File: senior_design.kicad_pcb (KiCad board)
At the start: 2 copper layers, 128.6 x 80.8 mm, 41 parts, among them J1 Conn_ARM_JTAG_SWD_20, J4 USB_B_Micro, U11 NCP1117-3.3_SOT223, U2 OPA196xDGK, U3 SM351LT, U4 OPA196xDGK, U6 STM32F469VETx

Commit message: layout work
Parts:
- removed C13, C14, C15, C16: .1uF, Capacitor_SMD:C_0805_2012Metric
- removed U3: SM351LT, Package_TO_SOT_SMD:SOT-23
- added J2: Conn_01x03_Pin, Connector_PinHeader_2.54mm:PinHeader_1x03_P2.54mm_Vertical, F.Cu at (189.5, 129.0)
- moved C4 46.0 mm to (205.6, 87.5)
- moved C3 42.9 mm to (197.0, 96.0), turned to -90 degrees
- moved C8 42.2 mm to (205.4, 83.5)
- moved C7 34.0 mm to (199.0, 73.0), turned to 90 degrees
- moved C2 29.7 mm to (182.5, 90.0), turned to 180 degrees
- moved C1 27.0 mm to (182.0, 83.5)
- moved C5 23.6 mm to (183.0, 87.5), turned to 180 degrees
- moved C11 22.4 mm to (187.5, 73.0), turned to 90 degrees
- moved R3 20.5 mm to (196.0, 118.0)
- moved R8 20.3 mm to (192.5, 107.0), turned to -90 degrees
- moved R4 18.3 mm to (188.5, 125.5), turned to -90 degrees
- moved C9 17.6 mm to (182.5, 77.5), turned to 180 degrees
- moved C12 16.8 mm to (182.5, 80.5), turned to 180 degrees
- moved R7 13.3 mm to (189.0, 110.5)
- moved C17 10.7 mm to (177.5, 70.5), turned to 180 degrees
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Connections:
- C5 pad 1: +3.3V -> Net-(U6-VDDA)
- U6 pad 28: unconnected-(U6-PA7-Pad28) -> ADC_IN1
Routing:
- net /MCU/SWCLK: track 0.00 -> 55.1 mm, vias 0 -> 1
- net GND: track 0.00 -> 50.6 mm, vias 0 -> 28
- net /MCU/SWDIO: track 0.00 -> 48.6 mm
- net +3.3V: track 0.00 -> 35.8 mm
- net ADC_IN1: track 0.00 -> 23.7 mm
- net +5V: track 0.00 -> 16.5 mm
- net Net-(U4-+): track 0.00 -> 15.8 mm
- net Net-(U2--): track 0.00 -> 10.1 mm
- net Net-(R11-Pad1): track 0.00 -> 8.77 mm
- net Net-(U2-+): track 0.00 -> 8.68 mm
- net Net-(U4--): track 0.00 -> 8.33 mm
- net Net-(U6-VDDA): track 0.00 -> 7.88 mm
- net Net-(J2-Pin_2): track 0.00 -> 4.61 mm
- net /MCU/SWD_RESET: track 0.00 -> 3.07 mm
- net Net-(D1-A): track 0.00 -> 2.85 mm
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- added copper zone on F.Cu, net +3.3V
- added copper zone on B.Cu, net GND

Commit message: schematic finish
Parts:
- added U3: RA8875, ra8875:RA8875, F.Cu at (229.9, 115.7)
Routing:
- net +5V: track 16.5 -> 88.0 mm, vias 0 -> 2
- net /MCU/SWCLK: vias 1 -> 2

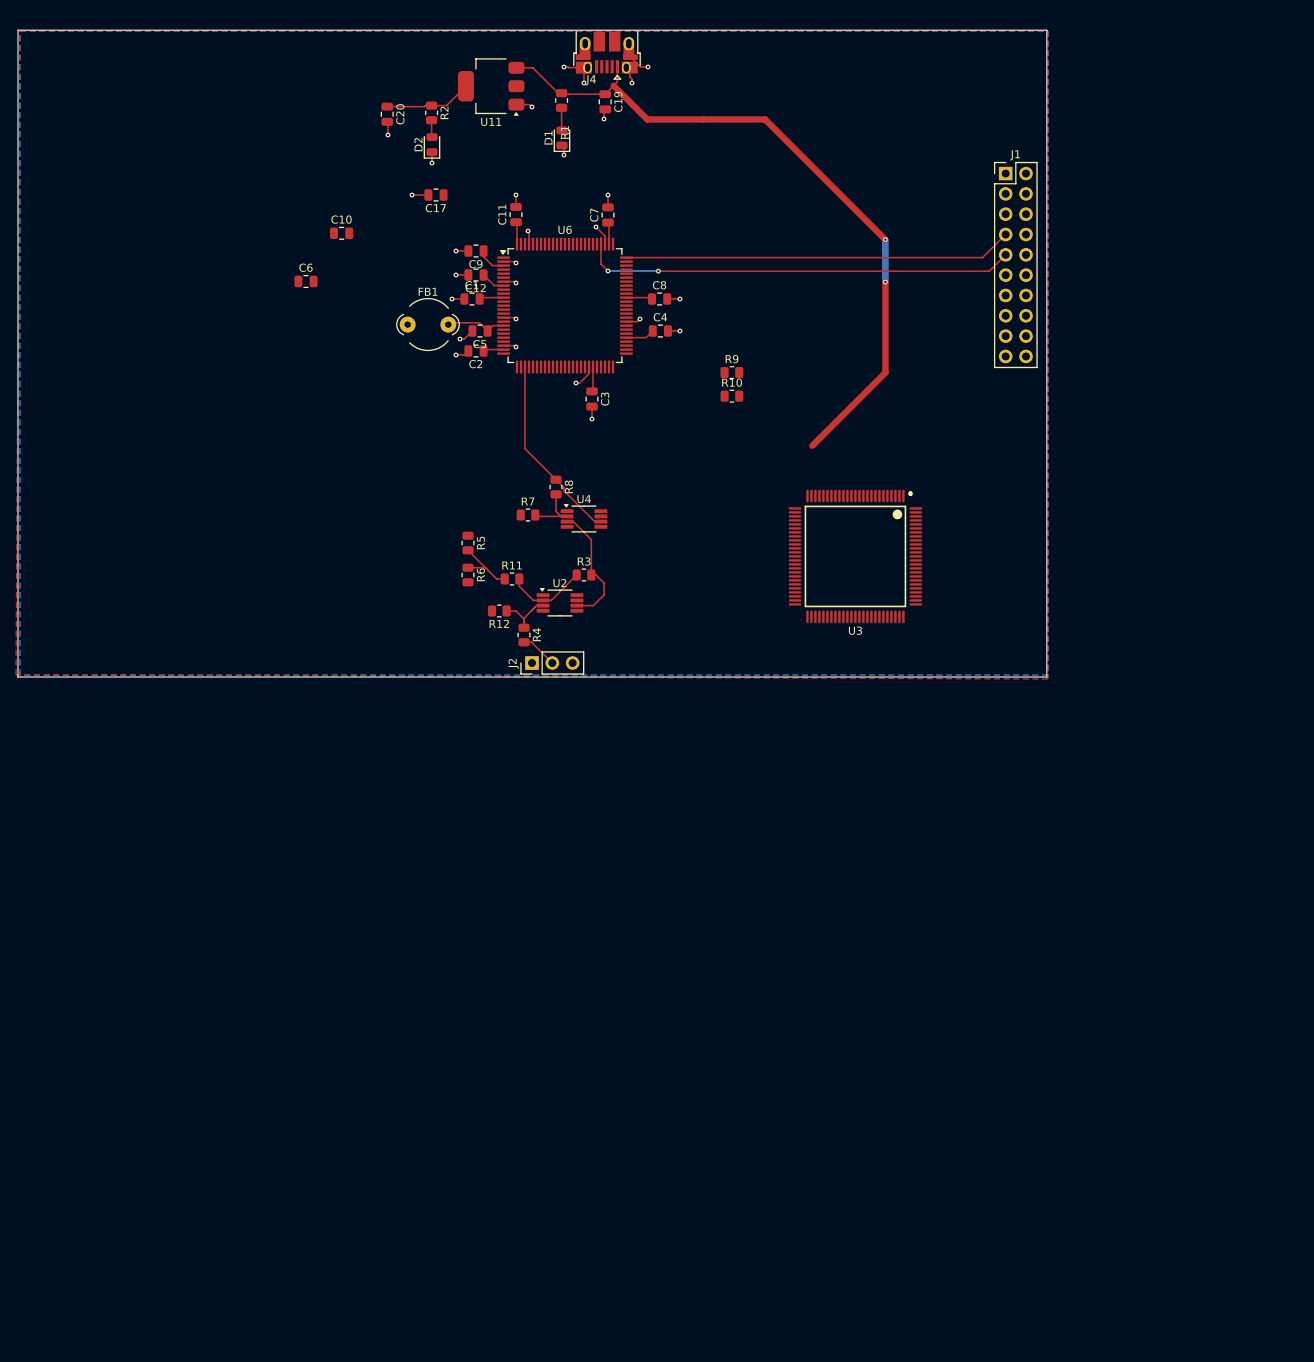
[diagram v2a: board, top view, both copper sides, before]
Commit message: initial display pcb
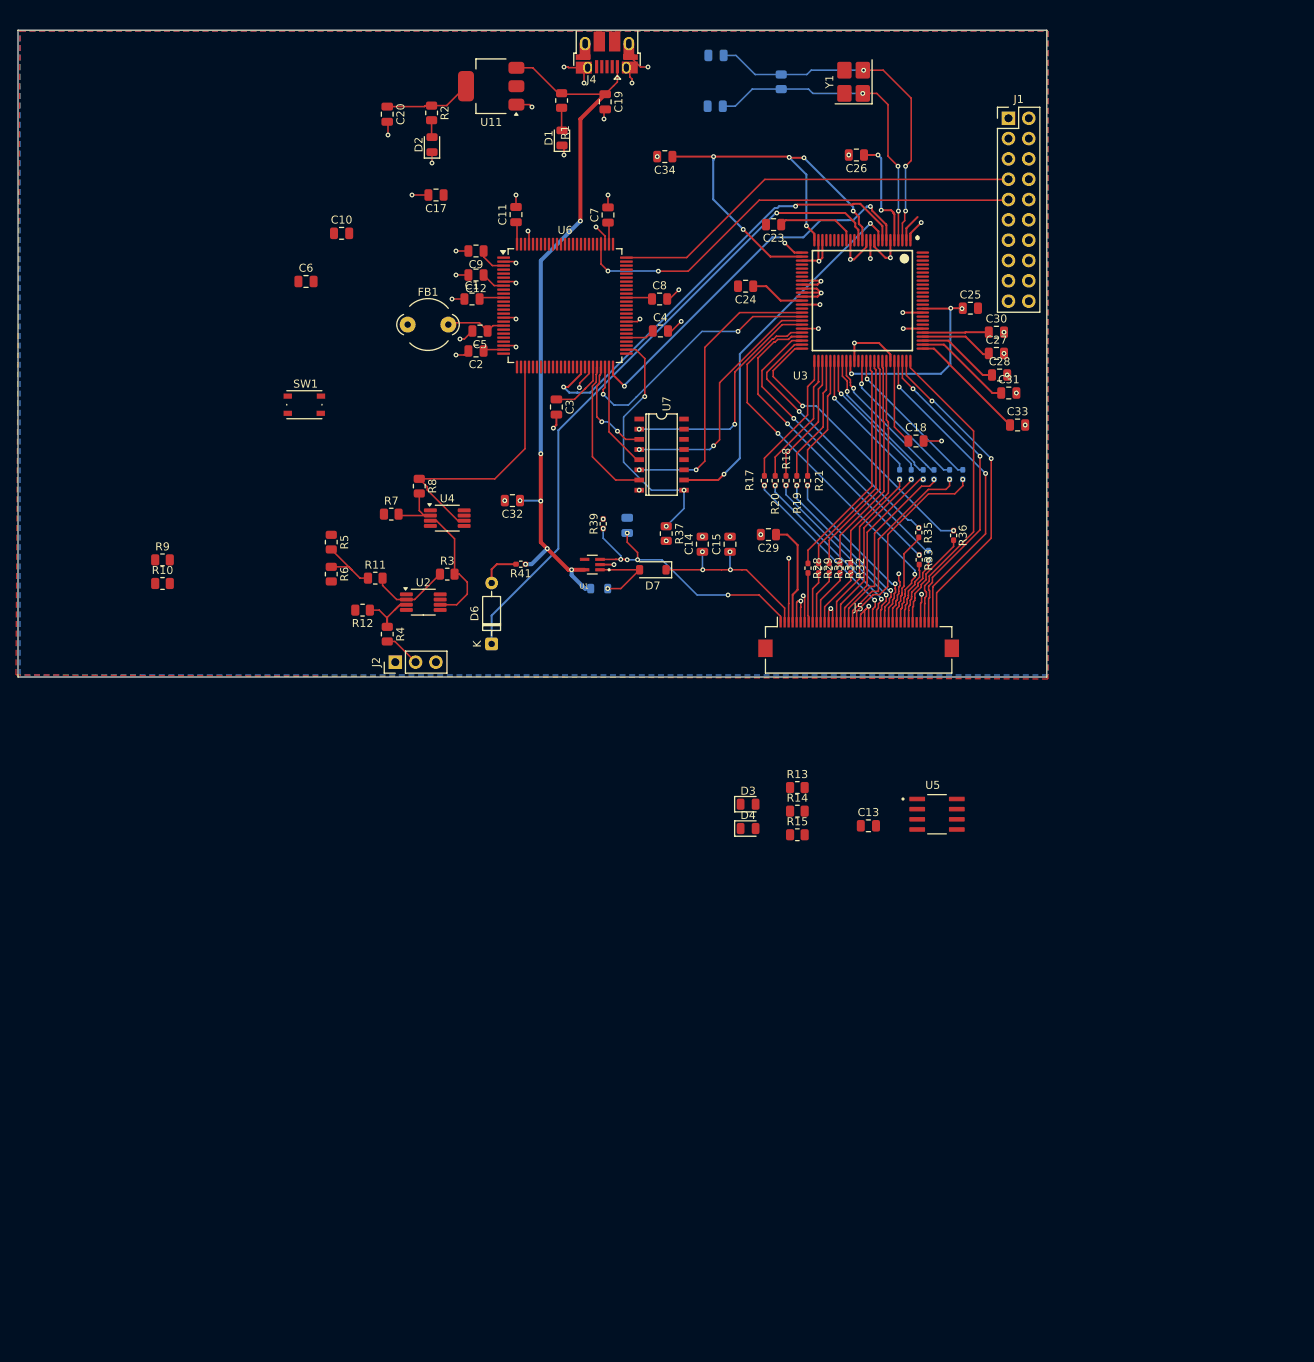
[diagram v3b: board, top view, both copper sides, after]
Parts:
- added C13: 4.7uF, Capacitor_SMD:C_0805_2012Metric, F.Cu at (231.6, 149.3)
- added C14: 1uF, Capacitor_SMD:C_0805_2012Metric, F.Cu at (210.8, 114.2)
- added C15: 1uF, Capacitor_SMD:C_0805_2012Metric, F.Cu at (214.2, 114.2)
- added C16: 0.1uF, Capacitor_SMD:C_0805_2012Metric, B.Cu at (201.4, 111.8)
- added C18: 0.1uF, Capacitor_SMD:C_0805_2012Metric, F.Cu at (237.5, 101.2)
- added C21: 15pF, Capacitor_SMD:C_0805_2012Metric, B.Cu at (212.5, 53.0)
- added C22: 15pF, Capacitor_SMD:C_0805_2012Metric, B.Cu at (212.4, 59.4)
- added C23: 0.1uF, Capacitor_SMD:C_0805_2012Metric, F.Cu at (219.7, 74.2)
- added C24: 0.1uF, Capacitor_SMD:C_0805_2012Metric, F.Cu at (216.2, 81.9)
- added C25: 0.1uF, Capacitor_SMD:C_0805_2012Metric, F.Cu at (244.3, 84.7)
- added C26: 0.1uF, Capacitor_SMD:C_0805_2012Metric, F.Cu at (230.1, 65.5)
- added C27: 1uF, Capacitor_SMD:C_0805_2012Metric, F.Cu at (247.6, 90.3)
- added C28: 0.1uF, Capacitor_SMD:C_0805_2012Metric, F.Cu at (247.9, 93.0)
- added C29: 0.1uF, Capacitor_SMD:C_0805_2012Metric, F.Cu at (219.1, 113.0)
- added C30: 0.1uF, Capacitor_SMD:C_0805_2012Metric, F.Cu at (247.6, 87.7)
- added C31: .01uF, Capacitor_SMD:C_0805_2012Metric, F.Cu at (249.1, 95.2)
- added C32: 10uF, Capacitor_SMD:C_0805_2012Metric, F.Cu at (187.1, 108.7)
- added C33: 0.1uF, Capacitor_SMD:C_0805_2012Metric, F.Cu at (250.2, 99.2)
- added C34: 0.1uF, Capacitor_SMD:C_0805_2012Metric, F.Cu at (206.1, 65.7)
- added D3: LED, LED_SMD:LED_0805_2012Metric, F.Cu at (216.5, 146.7)
- added D4: LED, LED_SMD:LED_0805_2012Metric, F.Cu at (216.5, 149.7)
- added D6: 1N4148, Diode_THT:D_DO-35_SOD27_P7.62mm_Horizontal, F.Cu at (184.4, 126.6)
- added D7: MBR0540, Diode_SMD:D_SOD-123, F.Cu at (204.6, 117.3)
- added J5: Out_to_display, Connector_FFC-FPC:Hirose_FH12-40S-0.5SH_1x40-1MP_P0.50mm_Horizontal, F.Cu at (230.3, 125.8)
- added L1: 6.8uH, Inductor_SMD:L_0805_2012Metric, B.Cu at (197.9, 119.7)
- added R13: 220, Resistor_SMD:R_0805_2012Metric, F.Cu at (222.7, 144.6)
- added R14: 220, Resistor_SMD:R_0805_2012Metric, F.Cu at (222.7, 147.5)
- added R15: 10k, Resistor_SMD:R_0805_2012Metric, F.Cu at (222.7, 150.5)
- added R17: 33, Resistor_SMD:R_0402_1005Metric_Pad0.72x0.64mm_HandSolder, F.Cu at (218.6, 106.2)
- added R18: 33, Resistor_SMD:R_0402_1005Metric_Pad0.72x0.64mm_HandSolder, F.Cu at (221.2, 106.2)
- added R19: 33, Resistor_SMD:R_0402_1005Metric_Pad0.72x0.64mm_HandSolder, F.Cu at (222.6, 106.2)
- added R20: 33, Resistor_SMD:R_0402_1005Metric_Pad0.72x0.64mm_HandSolder, F.Cu at (219.9, 106.2)
- added R21: 33, Resistor_SMD:R_0402_1005Metric_Pad0.72x0.64mm_HandSolder, F.Cu at (223.9, 106.2)
- added R22: 33, Resistor_SMD:R_0402_1005Metric_Pad0.72x0.64mm_HandSolder, B.Cu at (235.4, 105.5)
- added R23: 33, Resistor_SMD:R_0402_1005Metric_Pad0.72x0.64mm_HandSolder, B.Cu at (236.9, 105.5)
- added R24: 33, Resistor_SMD:R_0402_1005Metric_Pad0.72x0.64mm_HandSolder, B.Cu at (238.4, 105.5)
- added R25: 33, Resistor_SMD:R_0402_1005Metric_Pad0.72x0.64mm_HandSolder, B.Cu at (239.8, 105.5)
- added R26: 33, Resistor_SMD:R_0402_1005Metric_Pad0.72x0.64mm_HandSolder, B.Cu at (241.7, 105.5)
- added R27: 33, Resistor_SMD:R_0402_1005Metric_Pad0.72x0.64mm_HandSolder, B.Cu at (243.3, 105.5)
- added R28: 33, Resistor_SMD:R_0402_1005Metric_Pad0.72x0.64mm_HandSolder, F.Cu at (224.0, 117.1)
- added R29: 33, Resistor_SMD:R_0402_1005Metric_Pad0.72x0.64mm_HandSolder, F.Cu at (225.3, 117.1)
- added R30: 33, Resistor_SMD:R_0402_1005Metric_Pad0.72x0.64mm_HandSolder, F.Cu at (226.7, 117.1)
- added R31: 33, Resistor_SMD:R_0402_1005Metric_Pad0.72x0.64mm_HandSolder, F.Cu at (228.0, 117.1)
- added R32: 33, Resistor_SMD:R_0402_1005Metric_Pad0.72x0.64mm_HandSolder, F.Cu at (229.3, 117.2)
- added R33: 33, Resistor_SMD:R_0402_1005Metric_Pad0.72x0.64mm_HandSolder, F.Cu at (237.9, 116.1)
- added R34: 33, Resistor_SMD:R_0402_1005Metric_Pad0.72x0.64mm_HandSolder, B.Cu at (239.1, 115.5)
- added R35: 33, Resistor_SMD:R_0402_1005Metric_Pad0.72x0.64mm_HandSolder, F.Cu at (237.8, 112.7)
- added R36: 33, Resistor_SMD:R_0402_1005Metric_Pad0.72x0.64mm_HandSolder, F.Cu at (242.2, 113.0)
- added R37: 10k, Resistor_SMD:R_0805_2012Metric, F.Cu at (206.3, 112.8)
- added R38: R, Resistor_SMD:R_0805_2012Metric, B.Cu at (220.7, 56.4)
- added R39: 10k, Resistor_SMD:R_0402_1005Metric_Pad0.72x0.64mm_HandSolder, F.Cu at (198.4, 111.6)
- added R41: 10k, Resistor_SMD:R_0402_1005Metric_Pad0.72x0.64mm_HandSolder, F.Cu at (188.1, 116.7)
- added SW1: SW_SPST, Button_Switch_SMD:SW_Push_1P1T_NO_Vertical_Wuerth_434133025816, F.Cu at (161.0, 96.7)
- added U1: Boost Converter - TPS61169DCKR, TPS61169:SOT65P210X110-5N, F.Cu at (197.0, 116.7)
- added U5: M24C64-WMN6TP, EEProm Footprint:SOIC127P600X175-8N, F.Cu at (240.1, 147.9)
- added U7: 74HC4050D, 74HC4050:SO16, F.Cu at (205.7, 103.0)
- added Y1: 20MHz, Crystal:Crystal_SMD_3225-4Pin_3.2x2.5mm_HandSoldering, F.Cu at (229.7, 56.4)
- U3: value RA8875 -> RA8875L3N
- moved R10 74.9 mm to (143.3, 119.1)
- moved R9 74.9 mm to (143.3, 116.1)
- moved U3 32.0 mm to (230.8, 83.7)
- moved J2 17.1 mm to (172.4, 128.9)
- moved R11 17.1 mm to (169.9, 118.4)
- moved R12 17.1 mm to (168.3, 122.4)
- moved R3 17.1 mm to (178.9, 117.9)
- moved R4 17.1 mm to (171.4, 125.4)
- moved R5 17.1 mm to (164.4, 113.9)
- moved R6 17.1 mm to (164.4, 117.9)
- moved R7 17.1 mm to (171.9, 110.4)
- moved R8 17.1 mm to (175.4, 106.9)
- moved U2 17.1 mm to (175.9, 121.4)
- moved U4 17.1 mm to (178.9, 110.9)
- moved J1 6.92 mm to (249.1, 60.9)
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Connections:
- net Net-(U6-VDDA) renamed /MCU/VDDA
- U3 pad 1: (no net) -> GND
- U3 pad 10: (no net) -> GND
- U3 pad 100: (no net) -> unconnected-(U3-DB15-Pad100)
- U3 pad 11: (no net) -> GND
- U3 pad 12: (no net) -> GND
- U3 pad 13: (no net) -> +3.3V
- U3 pad 14: (no net) -> /Peripherals/PWM0
- U3 pad 15: (no net) -> unconnected-(U3-PWM2-Pad15)
- U3 pad 16: (no net) -> GND
- U3 pad 17: (no net) -> +1V5
- U3 pad 18: (no net) -> unconnected-(U3-SFCL-Pad18)
- U3 pad 19: (no net) -> unconnected-(U3-SFDI-Pad19)
- U3 pad 2: (no net) -> +3.3V
- U3 pad 20: (no net) -> unconnected-(U3-SFDO-Pad20)
- U3 pad 21: (no net) -> unconnected-(U3-~{SFCS0}-Pad21)
- U3 pad 22: (no net) -> unconnected-(U3-~{SFCS1}-Pad22)
- U3 pad 23: (no net) -> GND
- U3 pad 24: (no net) -> GND
- U3 pad 25: (no net) -> +3.3V
- U3 pad 26: (no net) -> GND
- U3 pad 27: (no net) -> +3.3V
- U3 pad 28: (no net) -> GND
- U3 pad 29: (no net) -> unconnected-(U3-KOUT3/GPO3-Pad29)
- U3 pad 3: (no net) -> /Peripherals/X_1
- U3 pad 30: (no net) -> unconnected-(U3-KOUT2/GPO2-Pad30)
- U3 pad 31: (no net) -> unconnected-(U3-KOUT1/GPO1-Pad31)
- U3 pad 32: (no net) -> unconnected-(U3-KOUT0/GPO0-Pad32)
- U3 pad 33: (no net) -> GND
- U3 pad 34: (no net) -> GND
- U3 pad 35: (no net) -> GND
- U3 pad 36: (no net) -> GND
- U3 pad 37: (no net) -> GND
- U3 pad 38: (no net) -> +1V5
- U3 pad 39: (no net) -> GND
- U3 pad 4: (no net) -> /Peripherals/X_0
- U3 pad 40: (no net) -> +3.3V
- U3 pad 41: (no net) -> /Peripherals/SPI_CS_3V
- U3 pad 42: (no net) -> /MCU/MISO
- U3 pad 43: (no net) -> /Peripherals/MOSI_3V
- U3 pad 44: (no net) -> /Peripherals/SPI_CLK_3V
- U3 pad 45: (no net) -> GND
- U3 pad 46: (no net) -> /Peripherals/ON/OFF
- U3 pad 47: (no net) -> Net-(U3-HSYNC)
- U3 pad 48: (no net) -> Net-(U3-VSYNC)
- U3 pad 49: (no net) -> Net-(U3-PCLK)
- U3 pad 5: (no net) -> +1V5
- U3 pad 50: (no net) -> Net-(U3-DE)
- U3 pad 51: (no net) -> Net-(U3-PDAT0)
- U3 pad 52: (no net) -> Net-(U3-PDAT1)
- U3 pad 53: (no net) -> Net-(U3-PDAT2)
- U3 pad 54: (no net) -> Net-(U3-PDAT3)
- U3 pad 55: (no net) -> Net-(U3-PDAT4)
- U3 pad 56: (no net) -> Net-(U3-PDAT5)
- U3 pad 57: (no net) -> Net-(U3-PDAT6)
- U3 pad 58: (no net) -> Net-(U3-PDAT7)
- U3 pad 59: (no net) -> Net-(U3-PDAT8)
- U3 pad 6: (no net) -> GND
- U3 pad 60: (no net) -> +1V5
- U3 pad 61: (no net) -> GND
- U3 pad 62: (no net) -> +3.3V
- U3 pad 63: (no net) -> Net-(U3-PDAT9)
- U3 pad 64: (no net) -> Net-(U3-PDAT10)
- U3 pad 65: (no net) -> Net-(U3-PDAT11)
- U3 pad 66: (no net) -> Net-(U3-PDAT12)
- U3 pad 67: (no net) -> Net-(U3-PDAT13)
- U3 pad 68: (no net) -> Net-(U3-PDAT14)
- U3 pad 69: (no net) -> Net-(U3-PDAT15)
- U3 pad 7: (no net) -> /MCU/WAIT
- U3 pad 70: (no net) -> GND
- U3 pad 71: (no net) -> Net-(U3-ADC_VREF)
- U3 pad 72: (no net) -> /Peripherals/X-
- U3 pad 73: (no net) -> /Peripherals/Y+
- U3 pad 74: (no net) -> /Peripherals/Y-
- U3 pad 75: (no net) -> /Peripherals/X+
- U3 pad 76: (no net) -> +3.3V
- U3 pad 77: (no net) -> +3.3V
- U3 pad 78: (no net) -> +3.3V
- U3 pad 79: (no net) -> +3.3V
- U3 pad 8: (no net) -> /MCU/INT
- U3 pad 80: (no net) -> +3.3V
- U3 pad 81: (no net) -> GND
- U3 pad 82: (no net) -> unconnected-(U3-DB0-Pad82)
- U3 pad 83: (no net) -> unconnected-(U3-DB1-Pad83)
- U3 pad 84: (no net) -> unconnected-(U3-DB2-Pad84)
- U3 pad 85: (no net) -> GND
- U3 pad 86: (no net) -> +1V5
- U3 pad 87: (no net) -> +3.3V
- U3 pad 88: (no net) -> unconnected-(U3-DB3-Pad88)
- U3 pad 89: (no net) -> unconnected-(U3-DB4-Pad89)
- U3 pad 9: (no net) -> Net-(U3-~{RST})
- U3 pad 90: (no net) -> unconnected-(U3-DB5-Pad90)
- U3 pad 91: (no net) -> unconnected-(U3-DB6-Pad91)
- U3 pad 92: (no net) -> unconnected-(U3-DB7-Pad92)
- U3 pad 93: (no net) -> unconnected-(U3-DB8-Pad93)
- U3 pad 94: (no net) -> unconnected-(U3-DB9-Pad94)
- U3 pad 95: (no net) -> unconnected-(U3-DB10-Pad95)
- U3 pad 96: (no net) -> unconnected-(U3-DB11-Pad96)
- U3 pad 97: (no net) -> unconnected-(U3-DB12-Pad97)
- U3 pad 98: (no net) -> unconnected-(U3-DB13-Pad98)
- U3 pad 99: (no net) -> unconnected-(U3-DB14-Pad99)
- U6 pad 37: unconnected-(U6-PE12-Pad37) -> /MCU/LED1
- U6 pad 42: unconnected-(U6-PB11-Pad42) -> /MCU/INT
- U6 pad 46: unconnected-(U6-PB12-Pad46) -> /MCU/CS
- U6 pad 47: unconnected-(U6-PB13-Pad47) -> /MCU/SCK
- U6 pad 48: unconnected-(U6-PB14-Pad48) -> /MCU/MISO
- U6 pad 49: unconnected-(U6-PB15-Pad49) -> /MCU/MOSI
- U6 pad 50: unconnected-(U6-PD8-Pad50) -> /MCU/WAIT
- U6 pad 52: unconnected-(U6-PD10-Pad52) -> /MCU/RESET
- U6 pad 90: unconnected-(U6-PD6-Pad90) -> /MCU/LED2
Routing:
- net +3.3V: track 35.8 -> 172.6 mm, vias 0 -> 7
- net GND: track 50.6 -> 150.3 mm, vias 28 -> 63
- net /Peripherals/PWM0: track 0.00 -> 81.4 mm, vias 0 -> 2
- net +1V5: track 0.00 -> 57.4 mm, vias 0 -> 5
- net /MCU/INT: track 0.00 -> 56.6 mm, vias 0 -> 2
- net /Peripherals/ON/OFF: track 0.00 -> 50.2 mm, vias 0 -> 2
- net /MCU/WAIT: track 0.00 -> 48.2 mm, vias 0 -> 2
- net Net-(U3-~{RST}): track 0.00 -> 46.7 mm, vias 0 -> 2
- net /Peripherals/X_1: track 0.00 -> 44.4 mm, vias 0 -> 3
- net /Peripherals/X-: track 0.00 -> 40.2 mm, vias 0 -> 2
- net /Peripherals/Y-: track 0.00 -> 40.0 mm, vias 0 -> 2
- net /Peripherals/X_0: track 0.00 -> 39.8 mm, vias 0 -> 3
- net Net-(U3-HSYNC): track 0.00 -> 39.6 mm, vias 0 -> 2
- net /Peripherals/Y+: track 0.00 -> 39.4 mm, vias 0 -> 2
- net /Peripherals/X+: track 0.00 -> 38.7 mm
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
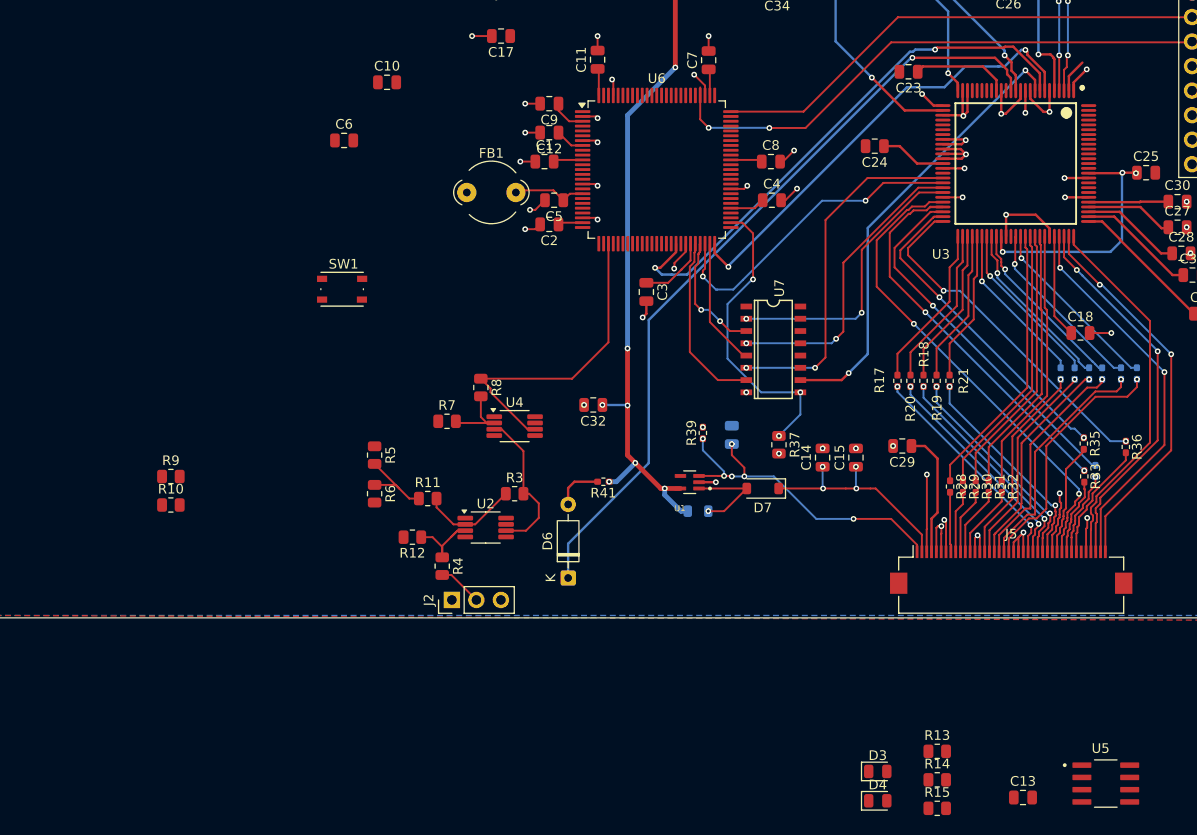
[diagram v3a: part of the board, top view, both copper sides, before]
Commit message: Updated EEProm PCB
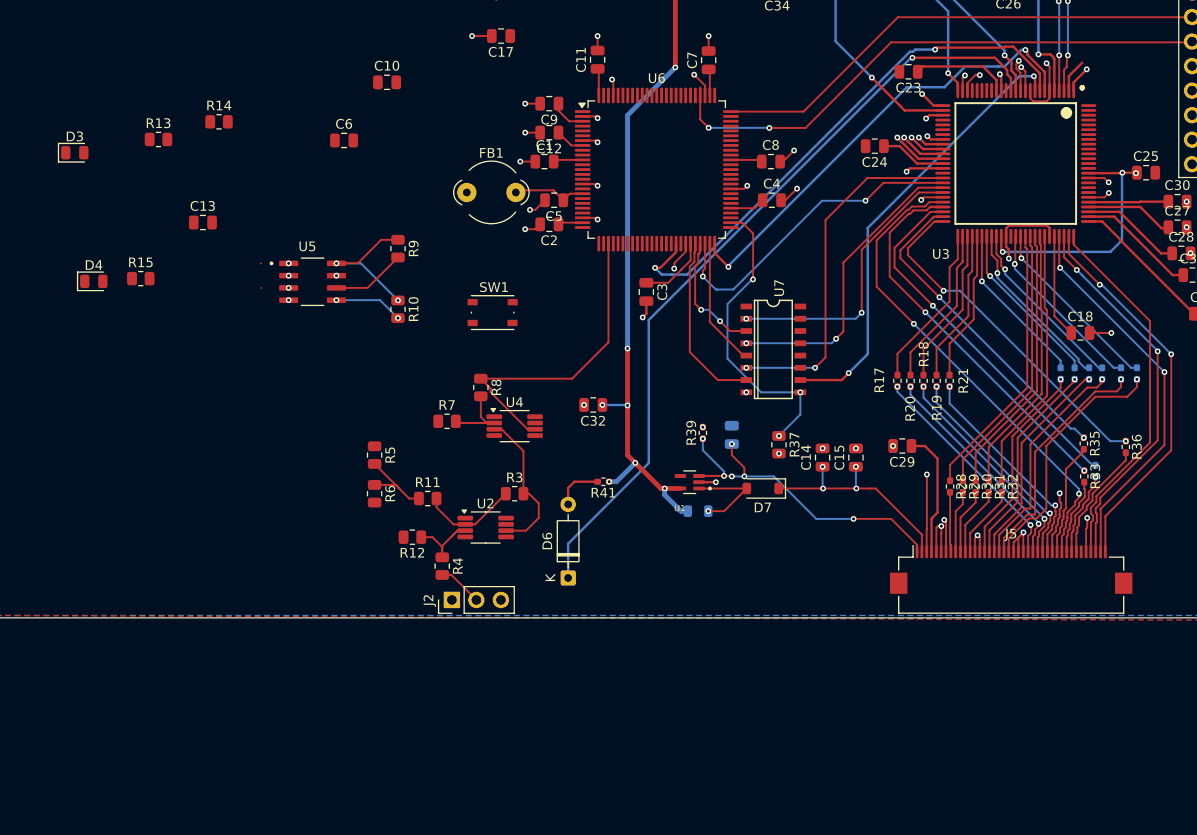
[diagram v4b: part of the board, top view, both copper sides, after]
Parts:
- moved D3 105.0 mm to (133.4, 82.6)
- moved C13 103.7 mm to (146.6, 89.8)
- moved R13 102.6 mm to (142.0, 81.2)
- moved R14 100.9 mm to (148.3, 79.4)
- moved R15 99.0 mm to (140.2, 95.6)
- moved D4 97.4 mm to (135.3, 95.9)
- moved U5 97.2 mm to (158.0, 95.9)
- moved R9 33.3 mm to (166.8, 92.5), turned to -90 degrees
- moved R10 31.0 mm to (166.8, 98.8), turned to -90 degrees
- moved SW1 15.8 mm to (176.6, 99.1)
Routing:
- net +3.3V: track 172.6 -> 188.0 mm, vias 7 -> 9
- net I2C1_SCL: track 0.00 -> 7.68 mm
- net GND: track 150.3 -> 157.7 mm, vias 63 -> 74
- net I2C1_SDA: track 0.00 -> 7.14 mm, vias 0 -> 2
